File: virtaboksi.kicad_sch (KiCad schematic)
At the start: 28 parts, among them J1 Panel_01x08, J2 Ext_01x05, J3 Powerpole 01x02, J4 Powerpole 01x02, J5 Powerpole 01x02, J6 Conn_01x03_Male, J7 TagConnect_TC2030-NL, U1 SRV05-4, U2 AMSRI-783.3-NZ, U3 STM8S003F3P, U4 SRV05-4, U5 SP3485EN

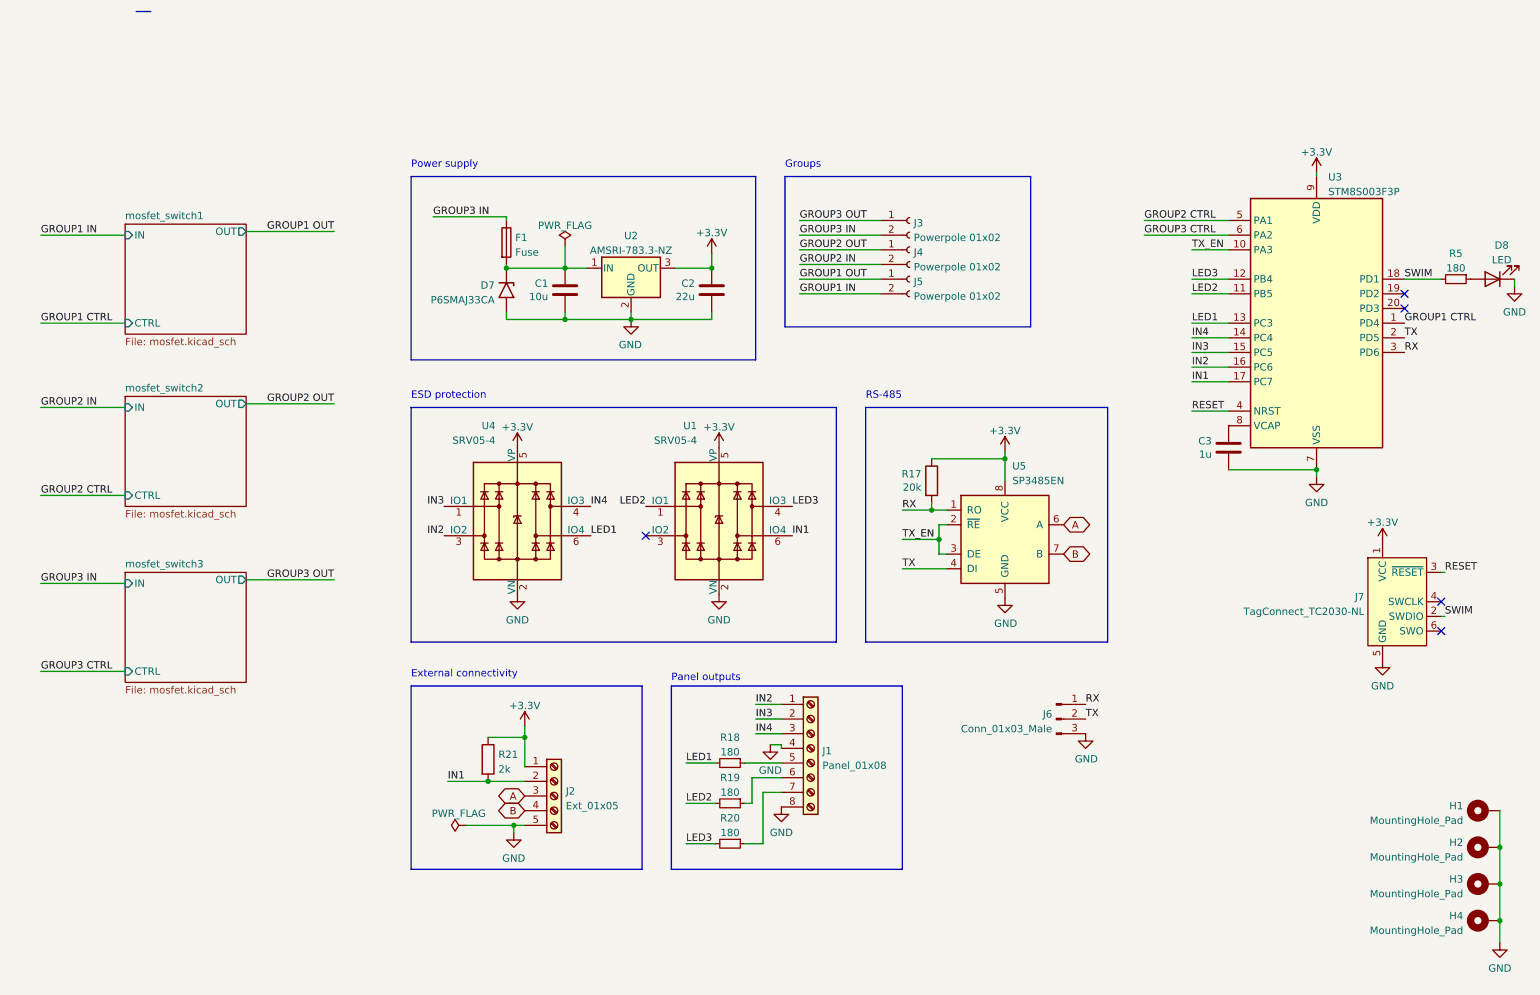
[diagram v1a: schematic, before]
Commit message: Update solder mask, do final tweaks, make it pass ERC & DRC
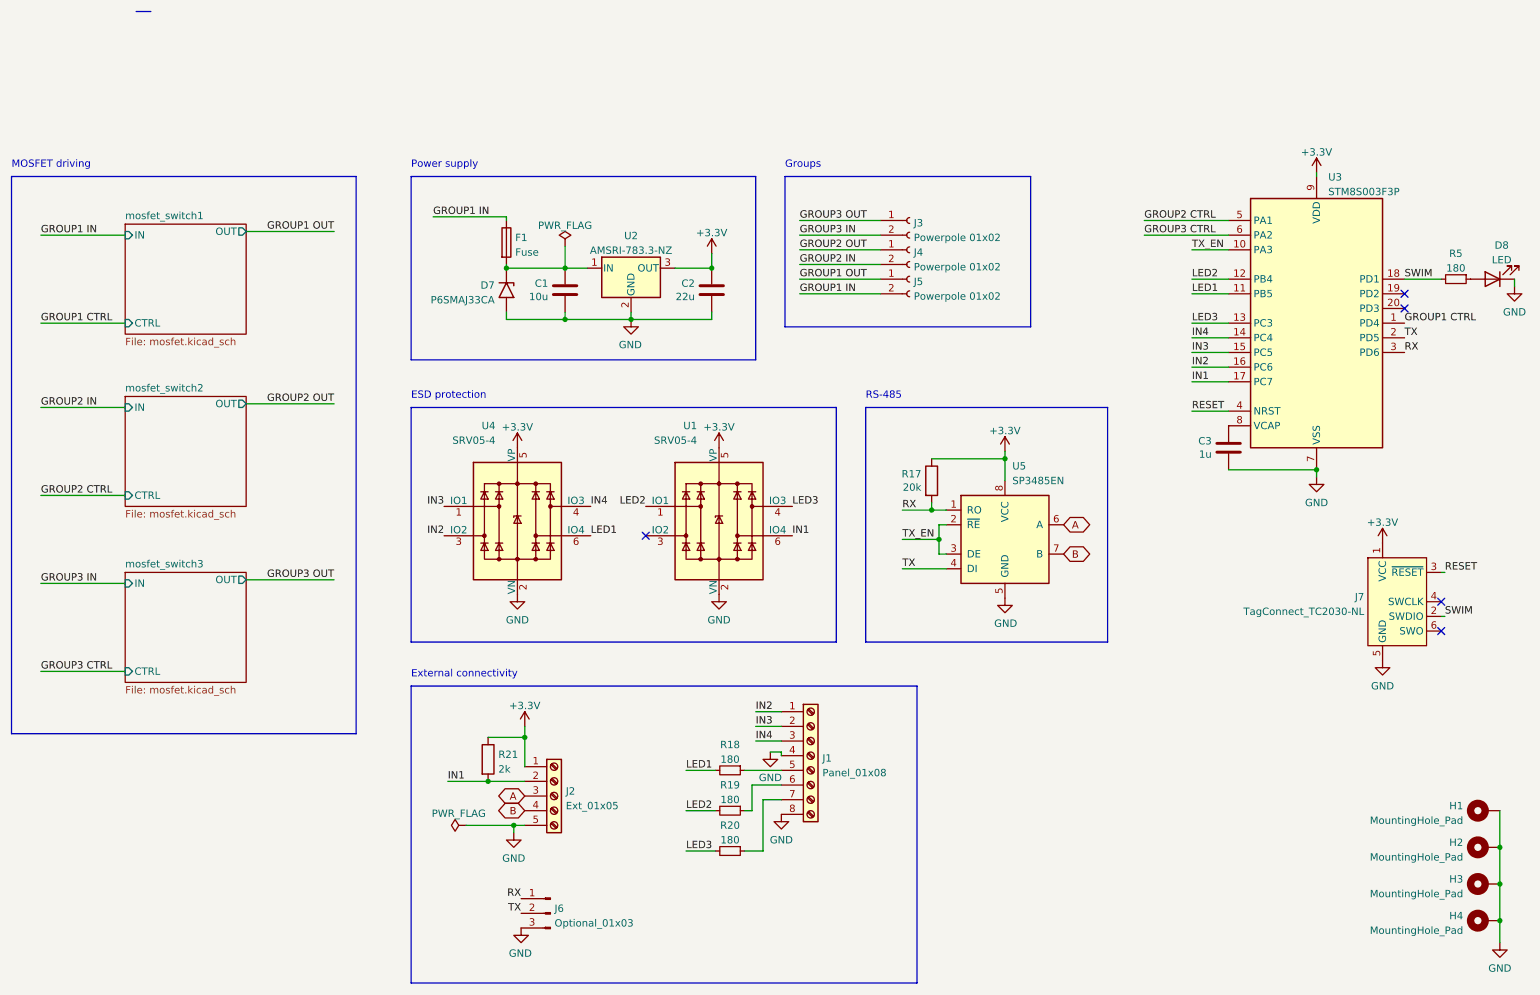
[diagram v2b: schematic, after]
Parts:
- J6: value Conn_01x03_Male -> Optional_01x03
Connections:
- net GROUP1 IN: now also F1.1
- net GROUP3 IN: no longer F1.1
- net LED1: now also U3.11 (PB5); no longer U3.13 (PC3)
- net LED2: now also U3.12 (PB4); no longer U3.11 (PB5)
- net LED3: now also U3.13 (PC3); no longer U3.12 (PB4)
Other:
- note added: "MOSFET driving"
- note removed: "Panel outputs"
- moved on the sheet: J1, J6, R18, R19, R20

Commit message: Reannotate everything
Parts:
- renumbered D7 to D1, D8 to D2, J6 to J1, J1 to J3, J3 to J4, J4 to J5, J5 to J6, R21 to R1, R18 to R2, R19 to R3, R20 to R4, R17 to R5, R5 to R6, U4 to U1, U1 to U3, U5 to U4, U3 to U5

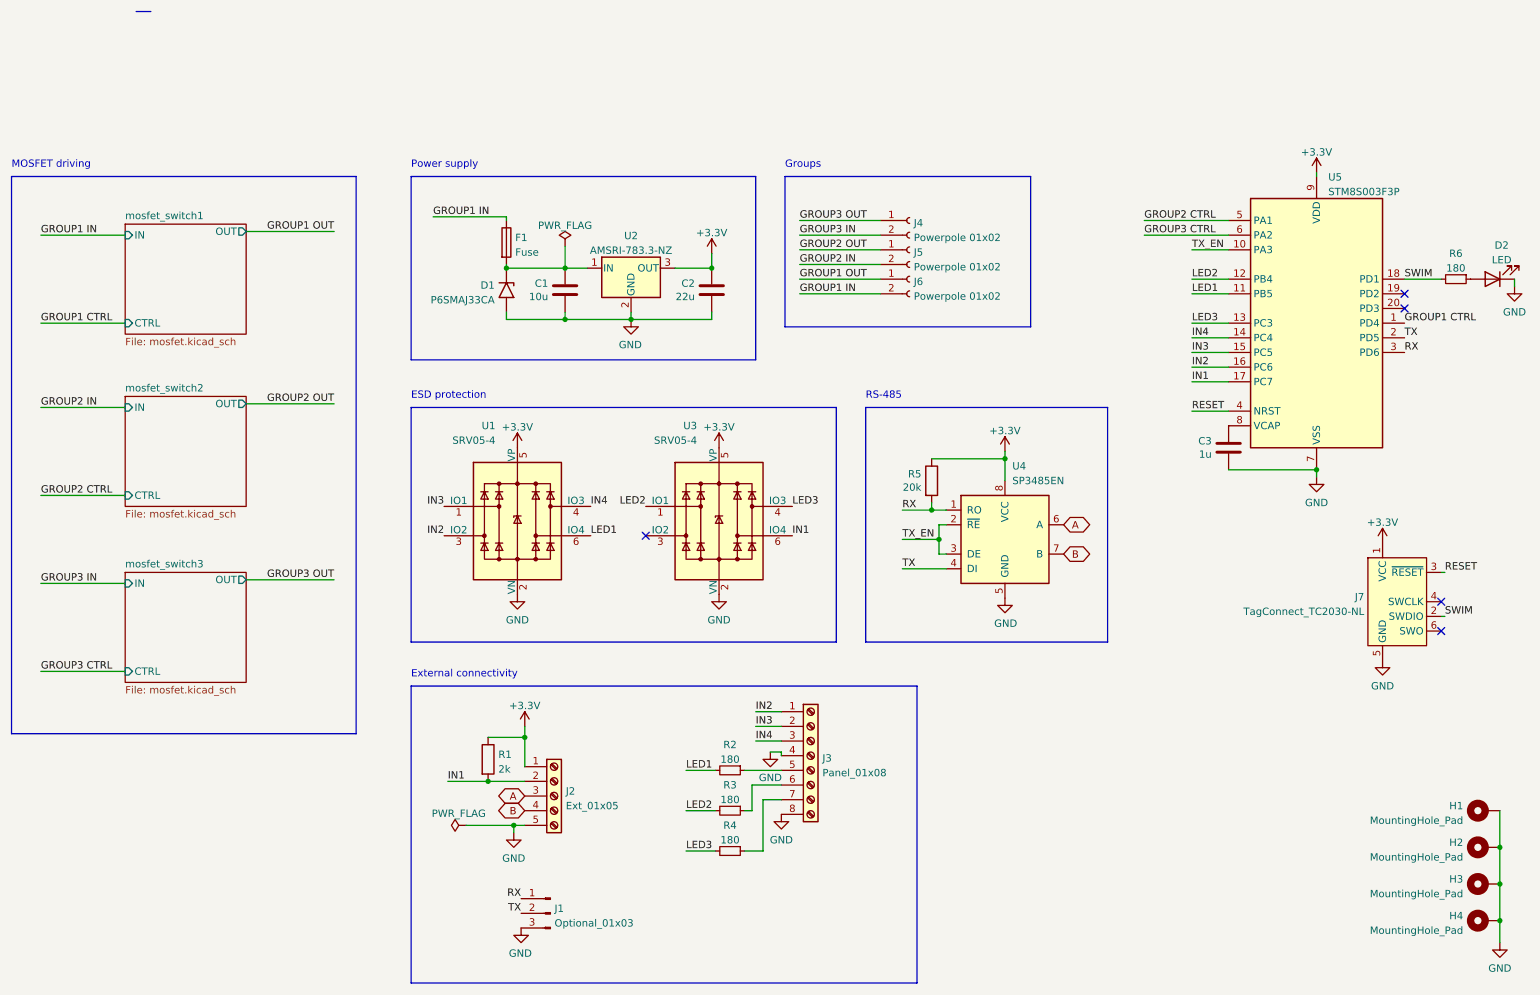
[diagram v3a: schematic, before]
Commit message: Throw fuse out of the window, clear space left of J2, add 2 extra pins
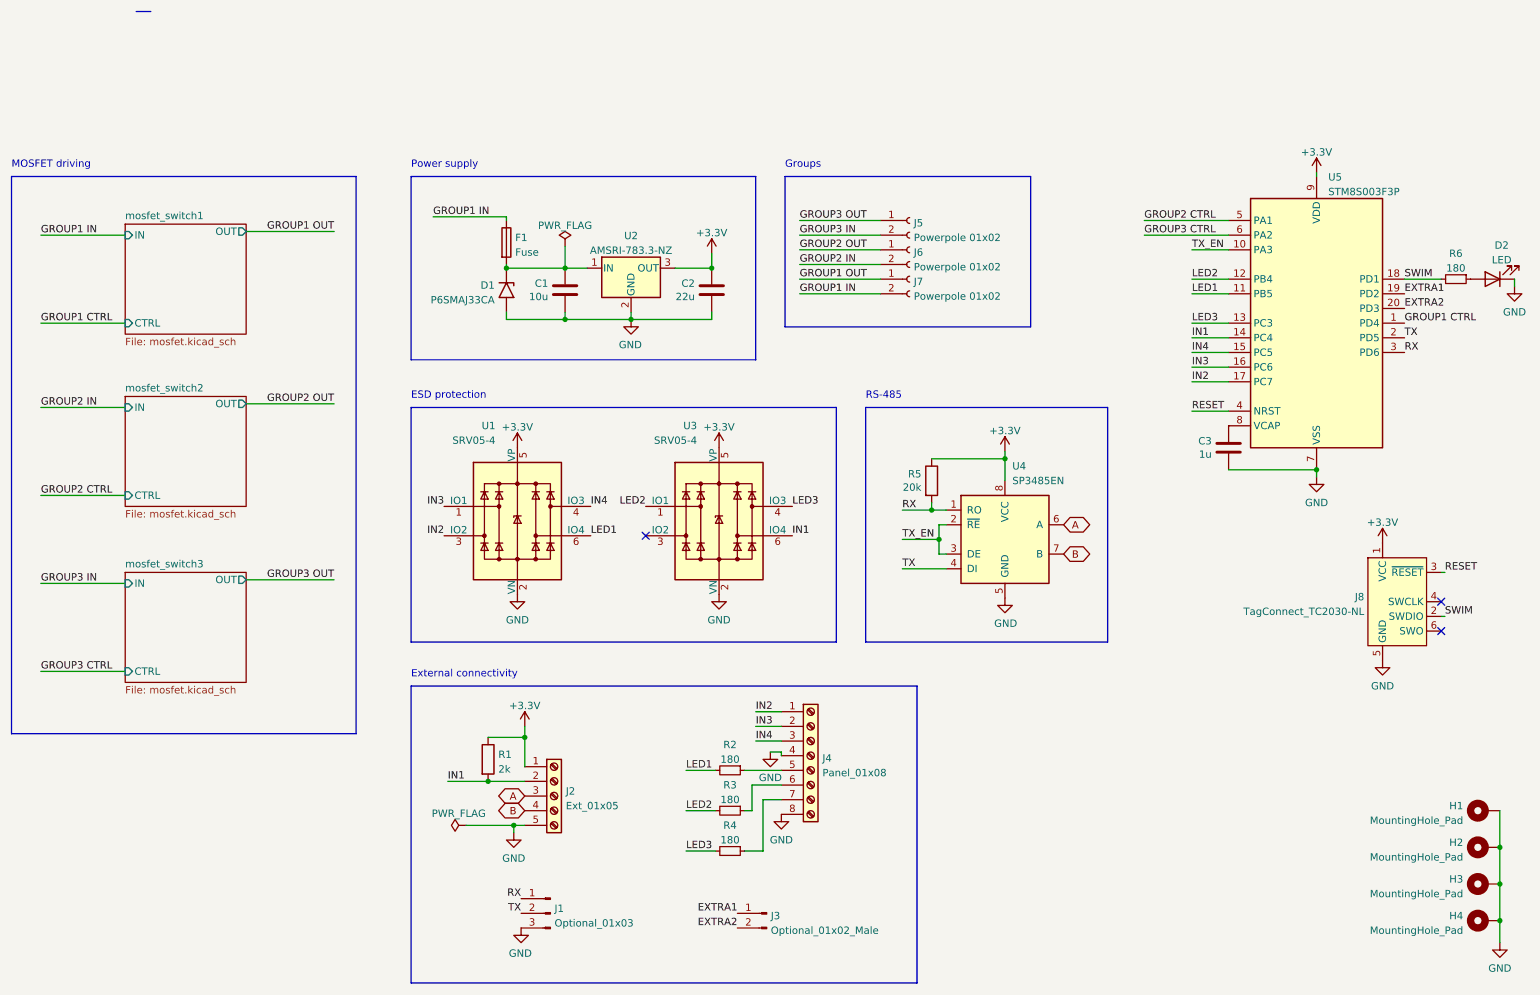
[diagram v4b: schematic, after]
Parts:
- added J3: Optional_01x02_Male, Connector_PinHeader_2.54mm:PinHeader_1x02_P2.54mm_Vertical, symbol Connector:Conn_01x02_Male
- F1: footprint Fuse:Fuse_0603_1608Metric_Pad1.05x0.95mm_HandSolder -> Connector_Wire:SolderWire-0.1sqmm_1x02_P3.6mm_D0.4mm_OD1mm
- renumbered J3 to J4, J4 to J5, J5 to J6, J6 to J7, J7 to J8
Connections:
- net IN1: now also U5.14 (PC4); no longer U5.17 (PC7)
- net IN2: now also U5.17 (PC7); no longer U5.16 (PC6)
- net IN3: now also U5.16 (PC6); no longer U5.15 (PC5)
- net IN4: now also U5.15 (PC5); no longer U5.14 (PC4)
- net EXTRA1: now reaches U5.19 (PD2)
- net EXTRA1: now also J3.1 (Pin_1)
- net EXTRA2: now reaches U5.20 (PD3)
- net EXTRA2: now also J3.2 (Pin_2)
- no-connect marks 5 -> 3
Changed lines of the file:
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@@
   (junction (at 116.205 37.465) (diameter 0) (color 0 0 0 0)
   )
-  (no_connect (at 261.62 44.45))
-  (no_connect (at 261.62 41.91))
   (no_connect (at 130.175 83.82))
   (no_connect (at 267.97 95.25))
@@
     (effects (font (size 1.27 1.27)) (justify left bottom))
   )
-  (label "IN3" (at 224.79 52.07 0)
-    (effects (font (size 1.27 1.27)) (justify left bottom))
+  (label "IN3" (at 224.79 54.61 0)
+    (effects (font (size 1.27 1.27)) (justify left bottom))
+  )
+  (label "EXTRA1" (at 146.05 149.225 180)
+    (effects (font (size 1.27 1.27)) (justify right bottom))
   )
   (label "SWIM" (at 261.62 39.37 0)
@@
     (effects (font (size 1.27 1.27)) (justify left bottom))
   )
-  (label "IN2" (at 224.79 54.61 0)
+  (label "IN2" (at 224.79 57.15 0)
     (effects (font (size 1.27 1.27)) (justify left bottom))
   )
@@
     (effects (font (size 1.27 1.27)) (justify left bottom))
   )
-  (label "IN1" (at 224.79 57.15 0)
+  (label "EXTRA1" (at 261.62 41.91 0)
+    (effects (font (size 1.27 1.27)) (justify left bottom))
+  )
+  (label "IN1" (at 224.79 49.53 0)
     (effects (font (size 1.27 1.27)) (justify left bottom))
   )
@@
     (effects (font (size 1.27 1.27)) (justify left bottom))
   )
-  (label "IN4" (at 224.79 49.53 0)
+  (label "IN4" (at 224.79 52.07 0)
     (effects (font (size 1.27 1.27)) (justify left bottom))
   )
@@
     (effects (font (size 1.27 1.27)) (justify left bottom))
   )
+  (label "EXTRA2" (at 261.62 44.45 0)
+    (effects (font (size 1.27 1.27)) (justify left bottom))
+  )
   (label "LED1" (at 224.79 41.91 0)
     (effects (font (size 1.27 1.27)) (justify left bottom))
@@
   (label "IN4" (at 120.65 78.74 0)
     (effects (font (size 1.27 1.27)) (justify left bottom))
+  )
+  (label "EXTRA2" (at 146.05 151.765 180)
+    (effects (font (size 1.27 1.27)) (justify right bottom))
   )
   (label "IN4" (at 149.225 119.38 0)
@@
   (symbol (lib_id "Connector:Screw_Terminal_01x08") (at 158.75 121.92 0) (unit 1)
     (in_bom yes) (on_board yes) (fields_autoplaced)
-    (property "Reference" "J3" (id 0) (at 160.782 122.3553 0)
+    (property "Reference" "J4" (id 0) (at 160.782 122.3553 0)
       (effects (font (size 1.27 1.27)) (justify left))
     )
@@
   (symbol (lib_id "Connector:Conn_01x02_Female") (at 175.895 34.29 0) (unit 1)
     (in_bom yes) (on_board yes) (fields_autoplaced)
-    (property "Reference" "J5" (id 0) (at 176.6062 34.7253 0)
+    (property "Reference" "J6" (id 0) (at 176.6062 34.7253 0)
       (effects (font (size 1.27 1.27)) (justify left))
     )
@@
   (symbol (lib_id "Connector:Conn_01x02_Female") (at 175.895 39.37 0) (unit 1)
     (in_bom yes) (on_board yes) (fields_autoplaced)
-    (property "Reference" "J6" (id 0) (at 176.6062 39.8053 0)
+    (property "Reference" "J7" (id 0) (at 176.6062 39.8053 0)
       (effects (font (size 1.27 1.27)) (justify left))
     )
@@
   (symbol (lib_id "Connector:Conn_01x02_Female") (at 175.895 29.21 0) (unit 1)
     (in_bom yes) (on_board yes) (fields_autoplaced)
-    (property "Reference" "J4" (id 0) (at 176.6062 29.6453 0)
+    (property "Reference" "J5" (id 0) (at 176.6062 29.6453 0)
       (effects (font (size 1.27 1.27)) (justify left))
     )
@@
   (symbol (lib_id "Connector:Conn_ARM_SWD_TagConnect_TC2030-NL") (at 260.35 95.25 0) (unit 1)
     (in_bom yes) (on_board yes) (fields_autoplaced)
-    (property "Reference" "J7" (id 0) (at 254.635 94.4153 0)
+    (property "Reference" "J8" (id 0) (at 254.635 94.4153 0)
       (effects (font (size 1.27 1.27)) (justify right))
     )
@@
       (effects (font (size 1.27 1.27)) (justify left))
     )
-    (property "Footprint" "Fuse:Fuse_0603_1608Metric_Pad1.05x0.95mm_HandSolder" (id 2) (at 104.267 33.02 90)
+    (property "Footprint" "Connector_Wire:SolderWire-0.1sqmm_1x02_P3.6mm_D0.4mm_OD1mm" (id 2) (at 104.267 33.02 90)
       (effects (font (size 1.27 1.27)) hide)
     )
     (property "Datasheet" "~" (id 3) (at 106.045 33.02 0)
+      (effects (font (size 1.27 1.27)) hide)
+    )
+    (pin "1")
+    (pin "2")
+  )
+  (symbol (lib_id "Connector:Conn_01x02_Male") (at 151.13 149.225 0) (mirror y) (unit 1)
+    (in_bom yes) (on_board yes) (fields_autoplaced)
+    (property "Reference" "J3" (id 0) (at 151.8412 149.6603 0)
+      (effects (font (size 1.27 1.27)) (justify right))
+    )
+    (property "Value" "Optional_01x02_Male" (id 1) (at 151.8412 152.1972 0)
+      (effects (font (size 1.27 1.27)) (justify right))
+    )
+    (property "Footprint" "Connector_PinHeader_2.54mm:PinHeader_1x02_P2.54mm_Vertical" (id 2) (at 151.13 149.225 0)
+      (effects (font (size 1.27 1.27)) hide)
+    )
+    (property "Datasheet" "~" (id 3) (at 151.13 149.225 0)
       (effects (font (size 1.27 1.27)) hide)
     )
@@
     )
     (path "/8f380f3a-9869-4d12-8165-58912a424229"
-      (reference "F1") (unit 1) (value "Fuse") (footprint "Fuse:Fuse_0603_1608Metric_Pad1.05x0.95mm_HandSolder")
+      (reference "F1") (unit 1) (value "Fuse") (footprint "Connector_Wire:SolderWire-0.1sqmm_1x02_P3.6mm_D0.4mm_OD1mm")
     )
     (path "/e28091c3-0a59-44fc-bcbf-5122b14ff16b"
@@
       (reference "J2") (unit 1) (value "Ext_01x05") (footprint "Connector_Phoenix_MC:PhoenixContact_MCV_1,5_5-G-3.5_1x05_P3.50mm_Vertical")
     )
+    (path "/91bec629-c4a6-47bd-a435-b57ee40d6d6b"
+      (reference "J3") (unit 1) (value "Optional_01x02_Male") (footprint "Connector_PinHeader_2.54mm:PinHeader_1x02_P2.54mm_Vertical")
+    )
     (path "/1bb20b60-c240-45a3-8b39-4a64e7d30638"
-      (reference "J3") (unit 1) (value "Panel_01x08") (footprint "Connector_Phoenix_MC:PhoenixContact_MCV_1,5_8-G-3.5_1x08_P3.50mm_Vertical")
+      (reference "J4") (unit 1) (value "Panel_01x08") (footprint "Connector_Phoenix_MC:PhoenixContact_MCV_1,5_8-G-3.5_1x08_P3.50mm_Vertical")
     )
     (path "/590d2007-4432-4cf1-bed4-e278a0f0bbe5"
-      (reference "J4") (unit 1) (value "Powerpole 01x02") (footprint "Powerpole:45A-VERT-PAIR")
+      (reference "J5") (unit 1) (value "Powerpole 01x02") (footprint "Powerpole:45A-VERT-PAIR")
     )
     (path "/31d335df-c0e7-4693-a236-f26680f3b2aa"
-      (reference "J5") (unit 1) (value "Powerpole 01x02") (footprint "Powerpole:45A-VERT-PAIR")
+      (reference "J6") (unit 1) (value "Powerpole 01x02") (footprint "Powerpole:45A-VERT-PAIR")
     )
     (path "/35ec96ad-af19-46e8-830d-87cfc8592b3e"
-      (reference "J6") (unit 1) (value "Powerpole 01x02") (footprint "Powerpole:45A-VERT-PAIR")
+      (reference "J7") (unit 1) (value "Powerpole 01x02") (footprint "Powerpole:45A-VERT-PAIR")
     )
     (path "/7e6505a7-6958-4f22-80f4-be0ec0e2a95a"
-      (reference "J7") (unit 1) (value "TagConnect_TC2030-NL") (footprint "Connector:Tag-Connect_TC2030-IDC-NL_2x03_P1.27mm_Vertical")
+      (reference "J8") (unit 1) (value "TagConnect_TC2030-NL") (footprint "Connector:Tag-Connect_TC2030-IDC-NL_2x03_P1.27mm_Vertical")
     )
     (path "/148741a4-2a3a-400f-b0f5-c870db1d25a5/baaf6e0a-52aa-41d8-82b3-125c4a4f9671"

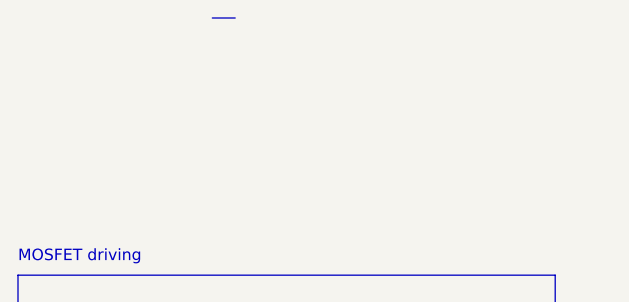
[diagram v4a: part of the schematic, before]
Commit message: Add makeshift fuse
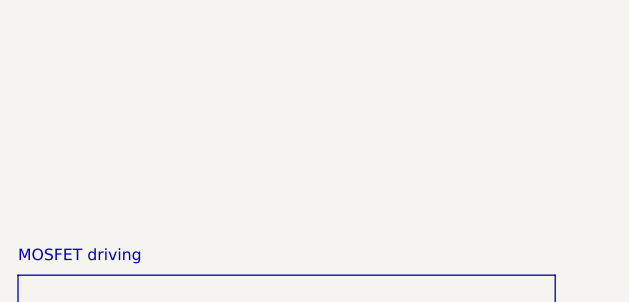
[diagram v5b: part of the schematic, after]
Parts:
- F1: footprint Connector_Wire:SolderWire-0.1sqmm_1x02_P3.6mm_D0.4mm_OD1mm -> Own parts:Fuse-kindof_1x02_P3.6mm_D0.4mm_OD1mm
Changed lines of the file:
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@@
-    (stroke (width 0) (type default) (color 0 0 0 0))
-  )
-  (polyline (pts (xy 41.91 -6.985) (xy 44.45 -6.985))
     (stroke (width 0) (type default) (color 0 0 0 0))
   )
@@
       (effects (font (size 1.27 1.27)) (justify left))
     )
-    (property "Footprint" "Connector_Wire:SolderWire-0.1sqmm_1x02_P3.6mm_D0.4mm_OD1mm" (id 2) (at 104.267 33.02 90)
+    (property "Footprint" "Own parts:Fuse-kindof_1x02_P3.6mm_D0.4mm_OD1mm" (id 2) (at 104.267 33.02 90)
       (effects (font (size 1.27 1.27)) hide)
     )
@@
     )
     (path "/8f380f3a-9869-4d12-8165-58912a424229"
-      (reference "F1") (unit 1) (value "Fuse") (footprint "Connector_Wire:SolderWire-0.1sqmm_1x02_P3.6mm_D0.4mm_OD1mm")
+      (reference "F1") (unit 1) (value "Fuse") (footprint "Own parts:Fuse-kindof_1x02_P3.6mm_D0.4mm_OD1mm")
     )
     (path "/e28091c3-0a59-44fc-bcbf-5122b14ff16b"
